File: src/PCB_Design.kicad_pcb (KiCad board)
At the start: 2 copper layers, 1 part, among them U1 ADS1298xPAG

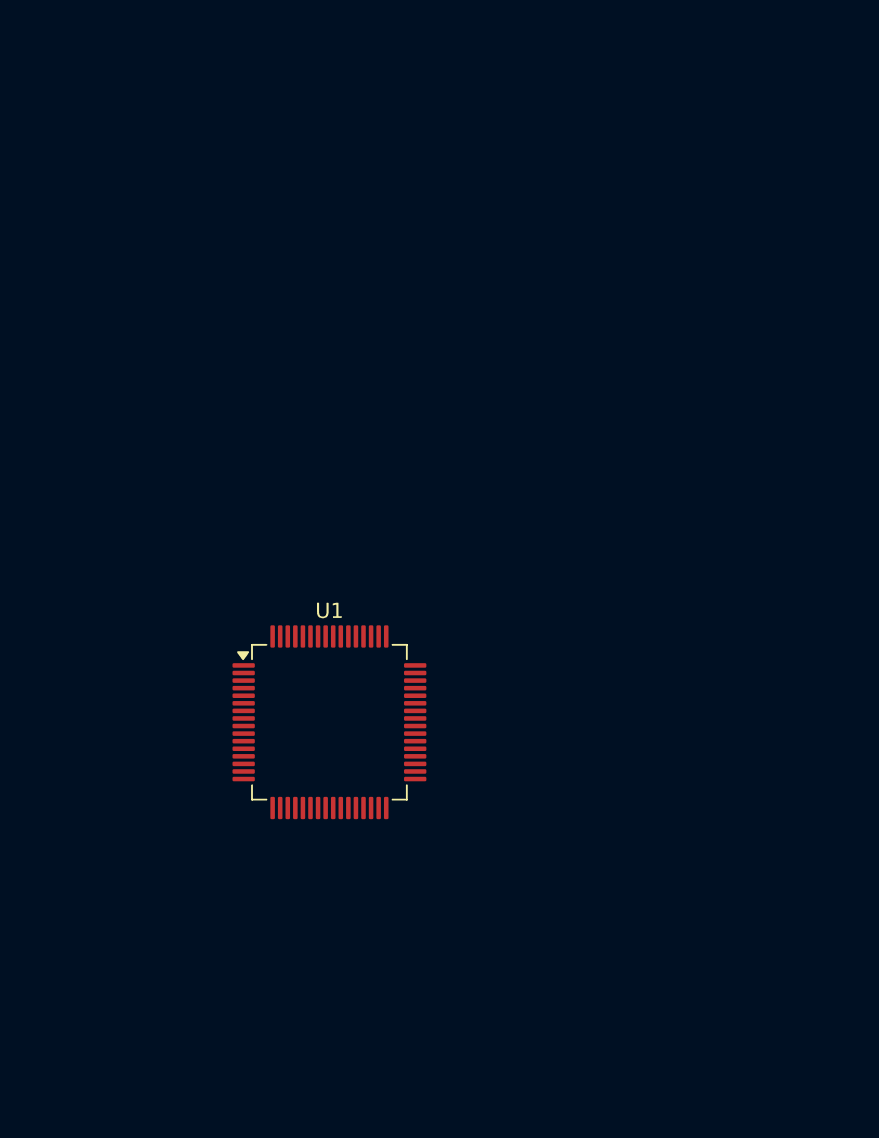
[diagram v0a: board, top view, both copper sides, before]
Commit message: Reverse Polarity Protection
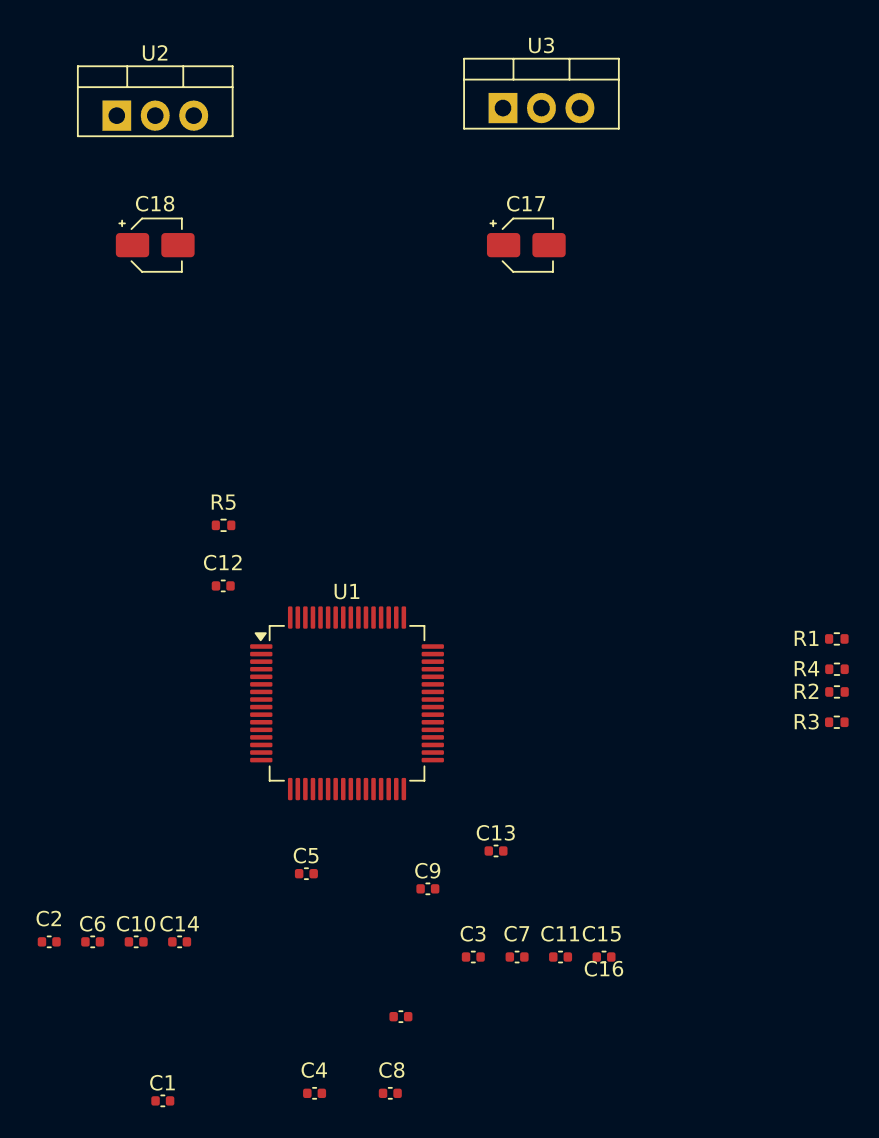
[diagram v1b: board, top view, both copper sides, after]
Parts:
- added C1: 100nF, Capacitor_SMD:C_0402_1005Metric, F.Cu at (142.0, 125.5)
- added C10: 1μF, Capacitor_SMD:C_0402_1005Metric, F.Cu at (140.2, 115.0)
- added C11: 0.1μF, Capacitor_SMD:C_0402_1005Metric, F.Cu at (168.3, 116.0)
- added C12: 1nF, Capacitor_SMD:C_0402_1005Metric, F.Cu at (146.0, 91.5)
- added C13: 0.1μF, Capacitor_SMD:C_0402_1005Metric, F.Cu at (164.0, 109.0)
- added C14: 10μF, Capacitor_SMD:C_0402_1005Metric, F.Cu at (143.1, 115.0)
- added C15: 1μF, Capacitor_SMD:C_0402_1005Metric, F.Cu at (171.1, 116.0)
- added C16: 1μF, Capacitor_SMD:C_0402_1005Metric, F.Cu at (157.7, 119.9)
- added C17: 10μF, Capacitor_SMD:CP_Elec_3x5.4, F.Cu at (166.0, 69.0)
- added C18: 10μF, Capacitor_SMD:CP_Elec_3x5.4, F.Cu at (141.5, 69.0)
- added C2: 1μF, Capacitor_SMD:C_0402_1005Metric, F.Cu at (134.5, 115.0)
- added C3: 1μF, Capacitor_SMD:C_0402_1005Metric, F.Cu at (162.5, 116.0)
- added C4: 100nF, Capacitor_SMD:C_0402_1005Metric, F.Cu at (152.0, 125.0)
- added C5: 0.1μF, Capacitor_SMD:C_0402_1005Metric, F.Cu at (151.5, 110.5)
- added C6: 0.1μF, Capacitor_SMD:C_0402_1005Metric, F.Cu at (137.4, 115.0)
- added C7: 100μF, Capacitor_SMD:C_0402_1005Metric, F.Cu at (165.4, 116.0)
- added C8: 1μF, Capacitor_SMD:C_0402_1005Metric, F.Cu at (157.0, 125.0)
- added C9: 1μF, Capacitor_SMD:C_0402_1005Metric, F.Cu at (159.5, 111.5)
- added R1: 10-kΩ, Resistor_SMD:R_0402_1005Metric, F.Cu at (186.5, 95.0)
- added R2: 10-kΩ, Resistor_SMD:R_0402_1005Metric, F.Cu at (186.5, 98.5)
- added R3: 10-kΩ, Resistor_SMD:R_0402_1005Metric, F.Cu at (186.5, 100.5)
- added R4: 10-kΩ, Resistor_SMD:R_0402_1005Metric, F.Cu at (186.5, 97.0)
- added R5: 1-MΩ, Resistor_SMD:R_0402_1005Metric, F.Cu at (146.0, 87.5)
- added U2: LM7805_TO220, Package_TO_SOT_THT:TO-220-3_Vertical, F.Cu at (139.0, 60.5)
- added U3: LD1117V33, Package_TO_SOT_THT:TO-220-3_Vertical, F.Cu at (164.5, 60.0)
- U1: value ADS1298xPAG -> ADS1299xPAG
- moved U1 1.71 mm to (154.2, 99.2)
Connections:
- net Net-(U1-DGND-Pad33) renamed DGND
- net Net-(U1-DVDD-Pad48) renamed /Regulator_3.3V
- U1 pad 1: unconnected-(U1-IN8N-Pad1) -> IN8N
- U1 pad 10: unconnected-(U1-IN4P-Pad10) -> IN4P
- U1 pad 11: unconnected-(U1-IN3N-Pad11) -> IN3N
- U1 pad 12: unconnected-(U1-IN3P-Pad12) -> IN3P
- U1 pad 13: unconnected-(U1-IN2N-Pad13) -> IN2N
- U1 pad 14: unconnected-(U1-IN2P-Pad14) -> IN2P
- U1 pad 15: unconnected-(U1-IN1N-Pad15) -> IN1P
- U1 pad 16: unconnected-(U1-IN1P-Pad16) -> IN1P
- U1 pad 17: unconnected-(U1-SRB1-Pad17) -> SRB1
- U1 pad 18: unconnected-(U1-SRB2-Pad18) -> SRB2
- U1 pad 19: Net-(U1-AVDD-Pad19) -> /Regulator_5V
- U1 pad 2: unconnected-(U1-IN8P-Pad2) -> IN8P
- U1 pad 20: Net-(U1-AVSS-Pad20) -> AVSS
- U1 pad 21: Net-(U1-AVDD-Pad19) -> /Regulator_5V
- U1 pad 22: Net-(U1-AVDD-Pad19) -> /Regulator_5V
- U1 pad 23: Net-(U1-AVSS-Pad20) -> AVSS
- U1 pad 24: unconnected-(U1-VREFP-Pad24) -> AVSS
- U1 pad 25: unconnected-(U1-VREFN-Pad25) -> Net-(U1-VREFN)
- U1 pad 26: unconnected-(U1-VCAP4-Pad26) -> Net-(U1-VCAP4)
- U1 pad 28: unconnected-(U1-VCAP1-Pad28) -> Net-(U1-VCAP1)
- U1 pad 3: unconnected-(U1-IN7N-Pad3) -> IN7N
- U1 pad 30: unconnected-(U1-VCAP2-Pad30) -> Net-(U1-VCAP2)
- U1 pad 31: unconnected-(U1-RESV1-Pad31) -> AGND
- U1 pad 32: Net-(U1-AVSS-Pad20) -> AVSS
- U1 pad 34: unconnected-(U1-DIN-Pad34) -> MOSI
- U1 pad 35: unconnected-(U1-~{PWDN}-Pad35) -> DVDD
- U1 pad 36: unconnected-(U1-~{RESET}-Pad36) -> RESET
- U1 pad 37: unconnected-(U1-CLK-Pad37) -> CLK
- U1 pad 39: unconnected-(U1-~{CS}-Pad39) -> CSI
- U1 pad 4: unconnected-(U1-IN7P-Pad4) -> IN7P
- U1 pad 40: unconnected-(U1-SCLK-Pad40) -> SCLK
- U1 pad 41: unconnected-(U1-DAISY_IN-Pad41) -> AGND
- U1 pad 42: unconnected-(U1-GPIO1-Pad42) -> Net-(U1-GPIO1)
- U1 pad 43: unconnected-(U1-DOUT-Pad43) -> MISO
- U1 pad 44: unconnected-(U1-GPIO2-Pad44) -> Net-(U1-GPIO2)
- U1 pad 45: unconnected-(U1-GPIO3-Pad45) -> Net-(U1-GPIO3)
- U1 pad 46: unconnected-(U1-GPIO4-Pad46) -> Net-(U1-GPIO4)
- U1 pad 47: unconnected-(U1-~{DRDY}-Pad47) -> DRDY
- U1 pad 5: unconnected-(U1-IN6N-Pad5) -> IN6N
- U1 pad 52: unconnected-(U1-CLKSEL-Pad52) -> DVDD
- U1 pad 53: unconnected-(U1-AVSS1-Pad53) -> AVSS
- U1 pad 54: unconnected-(U1-AVDD1-Pad54) -> /Regulator_5V
- U1 pad 55: unconnected-(U1-VCAP3-Pad55) -> Net-(U1-VCAP3)
- U1 pad 56: Net-(U1-AVDD-Pad19) -> /Regulator_5V
- U1 pad 57: Net-(U1-AVSS-Pad20) -> AVSS
- U1 pad 58: Net-(U1-AVSS-Pad20) -> AVSS
- U1 pad 59: Net-(U1-AVDD-Pad19) -> /Regulator_5V
- U1 pad 6: unconnected-(U1-IN6P-Pad6) -> IN6P
- U1 pad 60: unconnected-(U1-BIASREF-Pad60) -> AGND
- U1 pad 61: unconnected-(U1-BIASINV-Pad61) -> BIAS_INV
- U1 pad 62: unconnected-(U1-BIASIN-Pad62) -> Net-(U1-BIASIN)
- U1 pad 63: unconnected-(U1-BIASOUT-Pad63) -> Net-(U1-BIASIN)
- U1 pad 64: unconnected-(U1-RESERVED-Pad64) -> AGND
- U1 pad 7: unconnected-(U1-IN5N-Pad7) -> IN5N
- U1 pad 8: unconnected-(U1-IN5P-Pad8) -> IN5P
- U1 pad 9: unconnected-(U1-IN4N-Pad9) -> IN4N
